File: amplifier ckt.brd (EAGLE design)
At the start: 65.7 x 25.4 mm, 34 parts, among them U1 LM358DR

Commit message: added labels
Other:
- board size 65.7 x 25.4 mm -> 65.7 x 23.4 mm
- board text added: "+"
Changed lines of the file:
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@@
 <setting verticaltext="up"/>
 </settings>
-<grid distance="0.05" unitdist="inch" unit="inch" style="lines" multiple="1" display="no" altdistance="0.025" altunitdist="inch" altunit="inch"/>
+<grid distance="1" unitdist="mm" unit="mm" style="lines" multiple="1" display="no" altdistance="0.025" altunitdist="inch" altunit="inch"/>
 <layers>
 <layer number="1" name="Top" color="4" fill="1" visible="yes" active="yes"/>
@@
 <board>
 <plain>
-<wire x1="15.24" y1="17.78" x2="80.95" y2="17.78" width="0" layer="20"/>
-<wire x1="80.95" y1="17.78" x2="80.95" y2="43.17" width="0" layer="20"/>
-<wire x1="80.95" y1="43.17" x2="15.24" y2="43.17" width="0" layer="20"/>
-<wire x1="15.24" y1="43.17" x2="15.24" y2="17.78" width="0" layer="20"/>
-<dimension x1="15.24" y1="17.78" x2="80.95" y2="17.78" x3="48.095" y3="13.97" textsize="1.778" layer="1"/>
-<dimension x1="80.95" y1="43.17" x2="81.28" y2="17.78" x3="83.654571875" y3="30.50800625" textsize="1.778" layer="1"/>
+<wire x1="14.24" y1="19.78" x2="79.95" y2="19.78" width="0" layer="20"/>
+<wire x1="79.95" y1="19.78" x2="79.95" y2="43.17" width="0" layer="20"/>
+<wire x1="79.95" y1="43.17" x2="14.24" y2="43.17" width="0" layer="20"/>
+<wire x1="14.24" y1="43.17" x2="14.24" y2="19.78" width="0" layer="20"/>
+<text x="15.24" y="34.29" size="1.778" layer="25">+</text>
+<text x="46" y="39" size="1.778" layer="25">+</text>
 </plain>
 <attributes>
@@
 <wire x1="46.99" y1="35.56" x2="46.99" y2="30.48" width="0.254" layer="16"/>
 <polygon width="0.4064" layer="1">
-<vertex x="11.43" y="44.45"/>
-<vertex x="10.16" y="44.45"/>
-<vertex x="10.16" y="16.51"/>
+<vertex x="13.97" y="44.45"/>
+<vertex x="13.97" y="16.51"/>
 <vertex x="82.55" y="16.51"/>
 <vertex x="82.55" y="44.45"/>

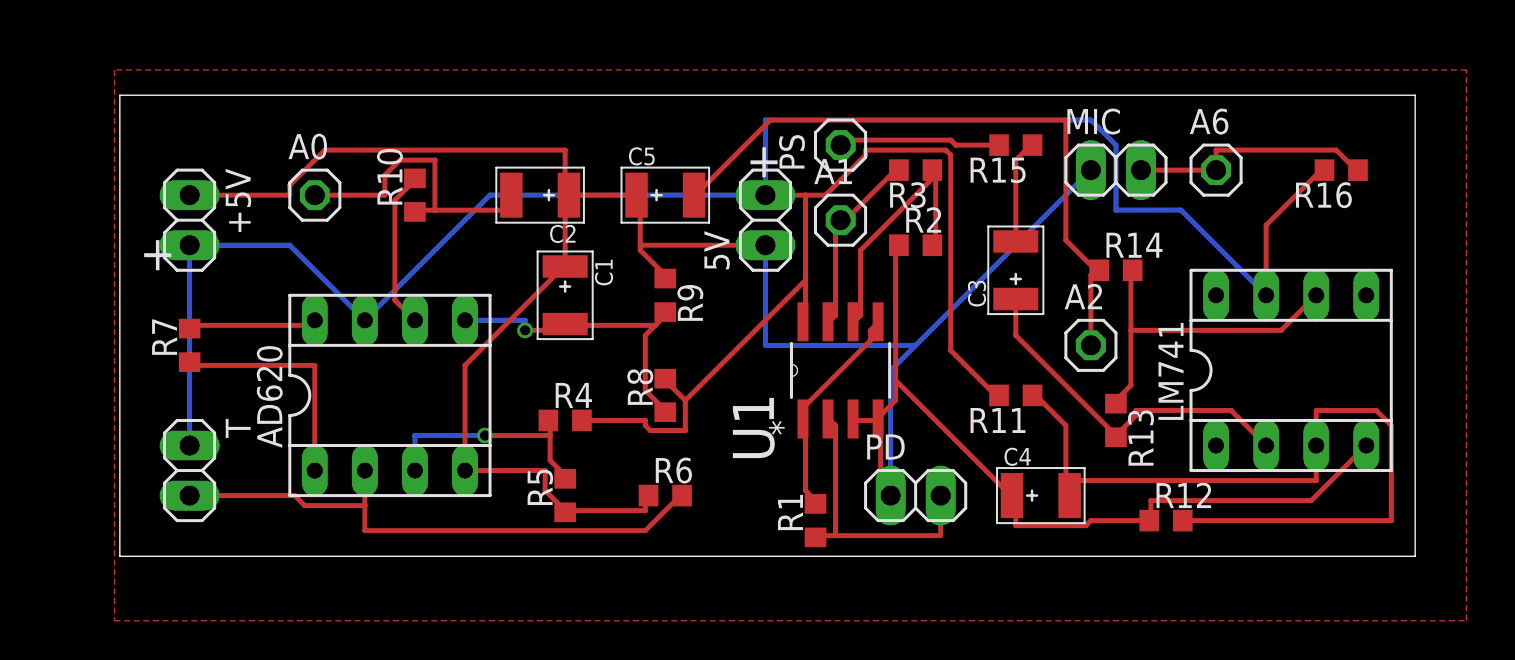
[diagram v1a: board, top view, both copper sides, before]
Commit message: new ckt with header pins
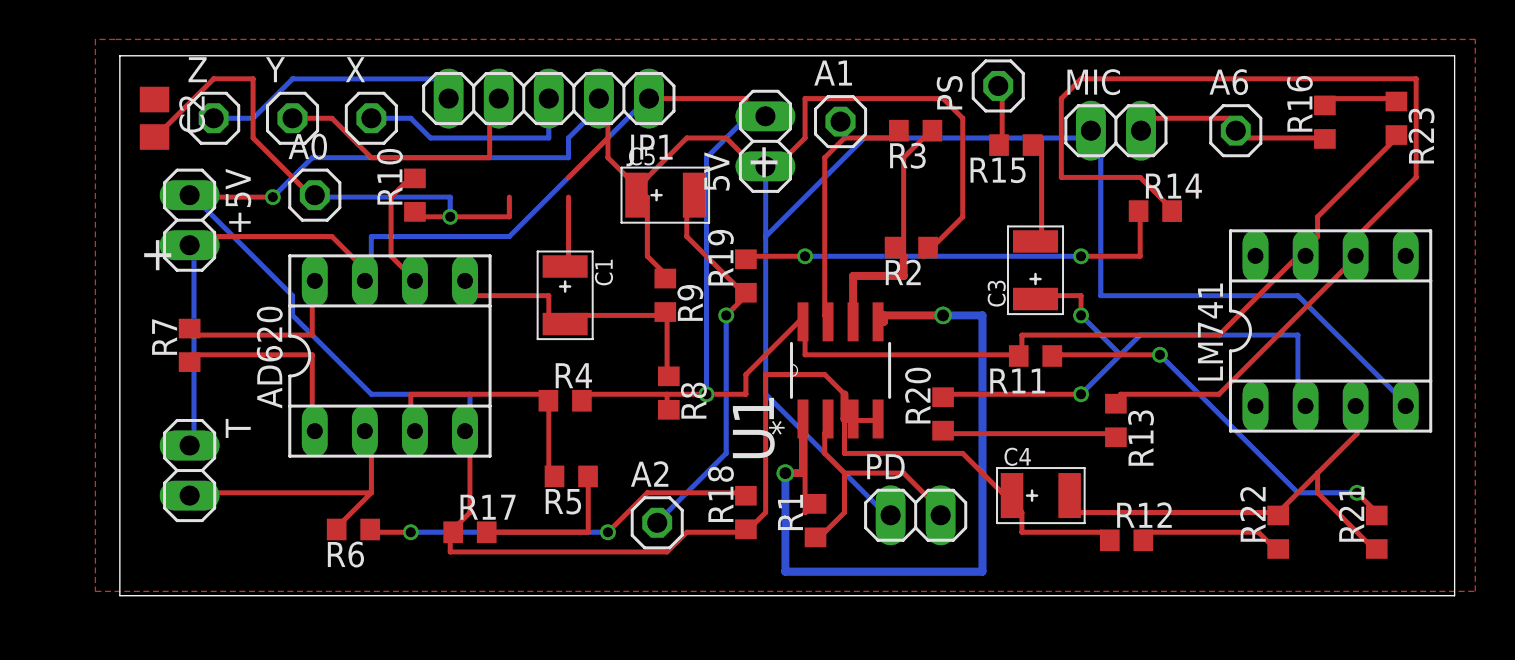
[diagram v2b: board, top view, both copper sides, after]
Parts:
- added JP1: (no value), pinhead:1X05
- added R17, R18, R19: 1.2k, rcl:R0603
- added R20: 200k, rcl:R0603
- added R21: 3k, rcl:R0603
- added R22: 15k, rcl:R0603
- added R23: 5.6k, rcl:R0603
- added X, Y, Z: (no value), pinhead:1X01
- C2: device OPL:AVX-B -> rcl:C0805
- R11: value 18k -> 15k
- R12: value 18k -> 3k
- R13: value 220k -> 20k
- R14, R5, R6: value 6.8k -> 5.6k
- R16: value 6.8k -> 1.2k
- moved A2 23.8 mm to (41.5, 21.5)
- moved C2 19.9 mm to (16.0, 42.0), turned to 270 degrees
- moved R6 15.9 mm to (26.1, 21.1), turned to 180 degrees
- moved PS 8.54 mm to (58.8, 43.6)
- moved A1 5.00 mm to (50.8, 41.8)
- moved 5V 4.00 mm to (47.0, 40.8)
- moved R14 3.61 mm to (66.8, 37.3)
- moved LM741 2.83 mm to (75.7, 31.2)
- moved R16 2.57 mm to (75.4, 41.8), turned to 90 degrees
- moved A6 2.24 mm to (70.8, 41.4)
- moved R11 2.24 mm to (60.7, 29.9)
- moved R12 2.24 mm to (65.3, 20.6)
- moved AD620 2.00 mm to (27.9, 29.9)
- moved MIC 2.00 mm to (64.8, 41.4)
- moved R3 2.00 mm to (54.6, 41.4)
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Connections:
- new net N$20: R17.2, R5.1
- new net N$21: R18.2, R6.1
- new net N$22: R13.2, R20.1
- new net N$23: R16.2, R23.1
- new net N$24: R11.1, R21.2
- new net N$25: R12.2, R22.1
- new net N$26: JP1.3, X.1
- new net N$27: JP1.4, Y.1
- new net N$28: JP1.5, Z.1
- new net N$7: R14.1, R19.2
- net GND: now also C2.1, JP1.2, R17.1, R18.1; no longer C2.+, R5.1, R6.1
- net N$12: now also C2.2; no longer C2.-
- net N$13: now also R21.1, R22.2; no longer R11.1, R12.2
- net N$16: now also R20.2; no longer R13.2
- net N$18: now also R19.1; no longer R14.1
- net VCC: now also JP1.1, R23.2; no longer R16.2
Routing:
- net GND: track 143.6 -> 215.6 mm, vias 0 -> 1
- net N$17: track 17.3 -> 55.5 mm
- net N$3: track 11.1 -> 42.7 mm, vias 0 -> 2
- net N$7: track 0.00 -> 22.5 mm, vias 0 -> 2
- net N$21: track 0.00 -> 20.1 mm, vias 0 -> 2
- net N$24: track 0.00 -> 19.9 mm, vias 0 -> 2
- net N$13: track 42.6 -> 24.6 mm
- net VCC: track 133.8 -> 116.3 mm, vias 0 -> 1
- net N$27: track 0.00 -> 14.3 mm
- net N$28: track 0.00 -> 13.9 mm
- net N$6: track 29.0 -> 15.7 mm
- net N$18: track 32.8 -> 20.2 mm, vias 0 -> 1
- net N$12: track 15.7 -> 28.2 mm, vias 0 -> 1
- net N$26: track 0.00 -> 11.4 mm
- net N$16: track 18.1 -> 29.3 mm, vias 0 -> 2
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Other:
- board size 65.7 x 23.4 mm -> 67.7 x 27.4 mm
